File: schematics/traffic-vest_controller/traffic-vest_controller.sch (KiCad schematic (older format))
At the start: 21 parts

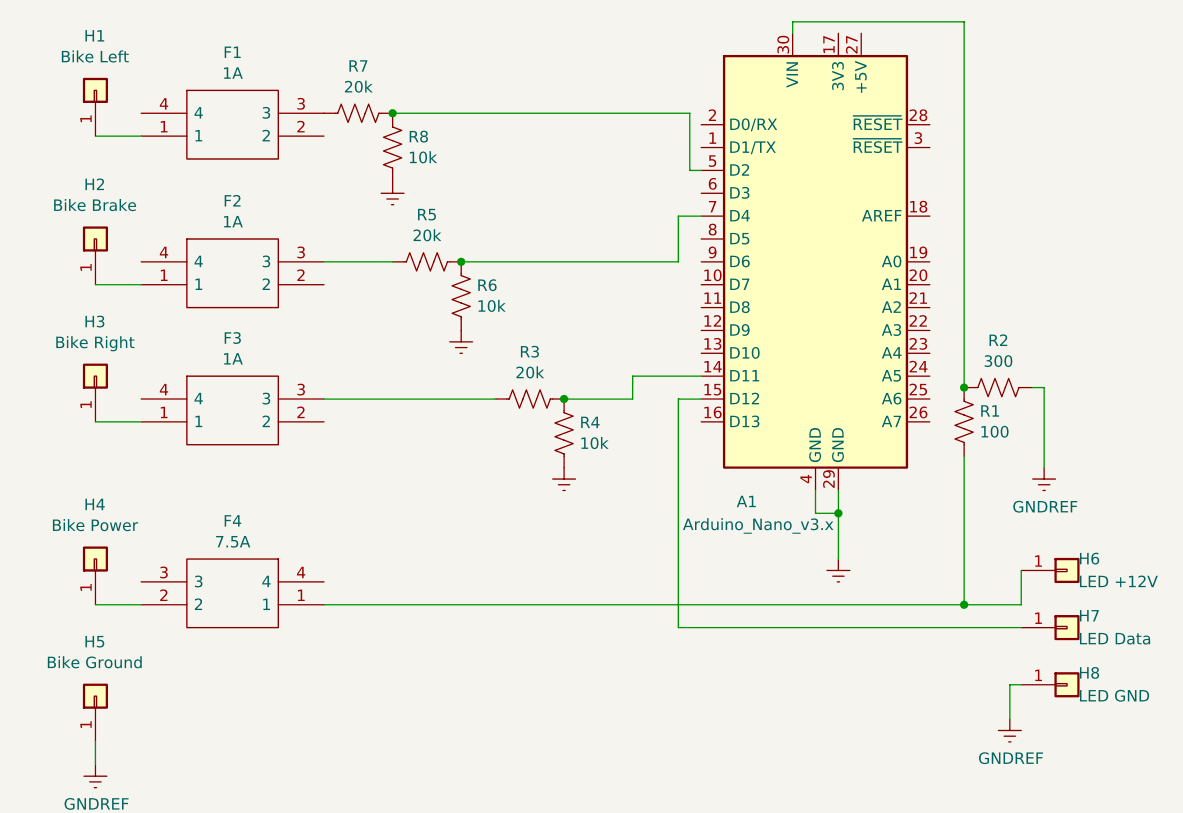
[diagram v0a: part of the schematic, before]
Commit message: expanded board footprint to accomodate corner mounting holes; rearranged fuses and pins for left/right to D2, D3 for external interrupts; fixed orientation of fuse clips
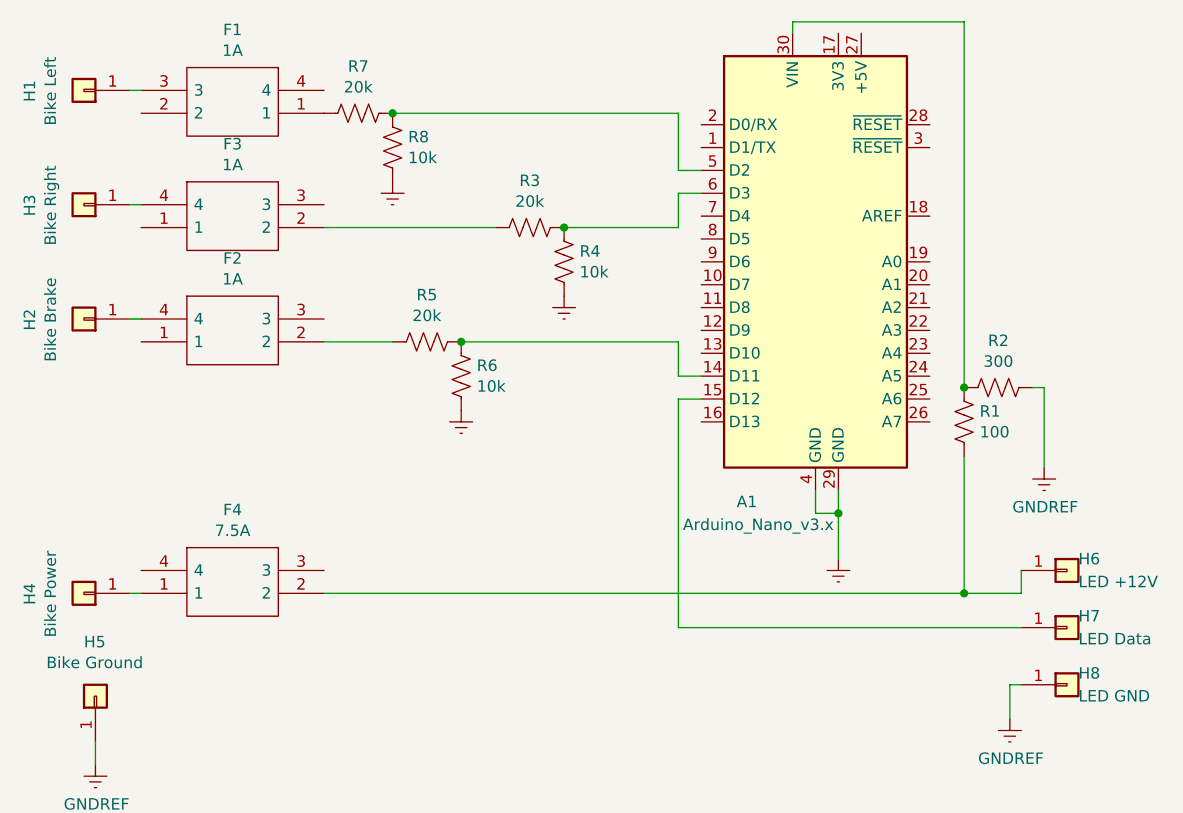
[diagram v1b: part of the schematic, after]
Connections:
- net at R3.1, R4.1: now also A1.6 (D3); no longer A1.14 (D11)
- net at R5.1, R6.1: now also A1.14 (D11); no longer A1.7 (D4)
- net at R7.2: now also F1.1; no longer F1.3
- net at R5.2: now also F2.2; no longer F2.3
- net at R3.2: now also F3.2; no longer F3.3
- net at H6.1 (Pin_1), R1.2: now also F4.2; no longer F4.1
- net at H1.1 (Pin_1): now also F1.3; no longer F1.1
- net at F2.1: no longer H2.1 (Pin_1)
- net at F2.4: now also H2.1 (Pin_1)
- net at F3.1: no longer H3.1 (Pin_1)
- net at F3.4: now also H3.1 (Pin_1)
- net at H4.1 (Pin_1): now also F4.1; no longer F4.2
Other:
- moved on the sheet: F1, F2, F3, F4, H1, H2, H3, H4, R3, R4, R5, R6

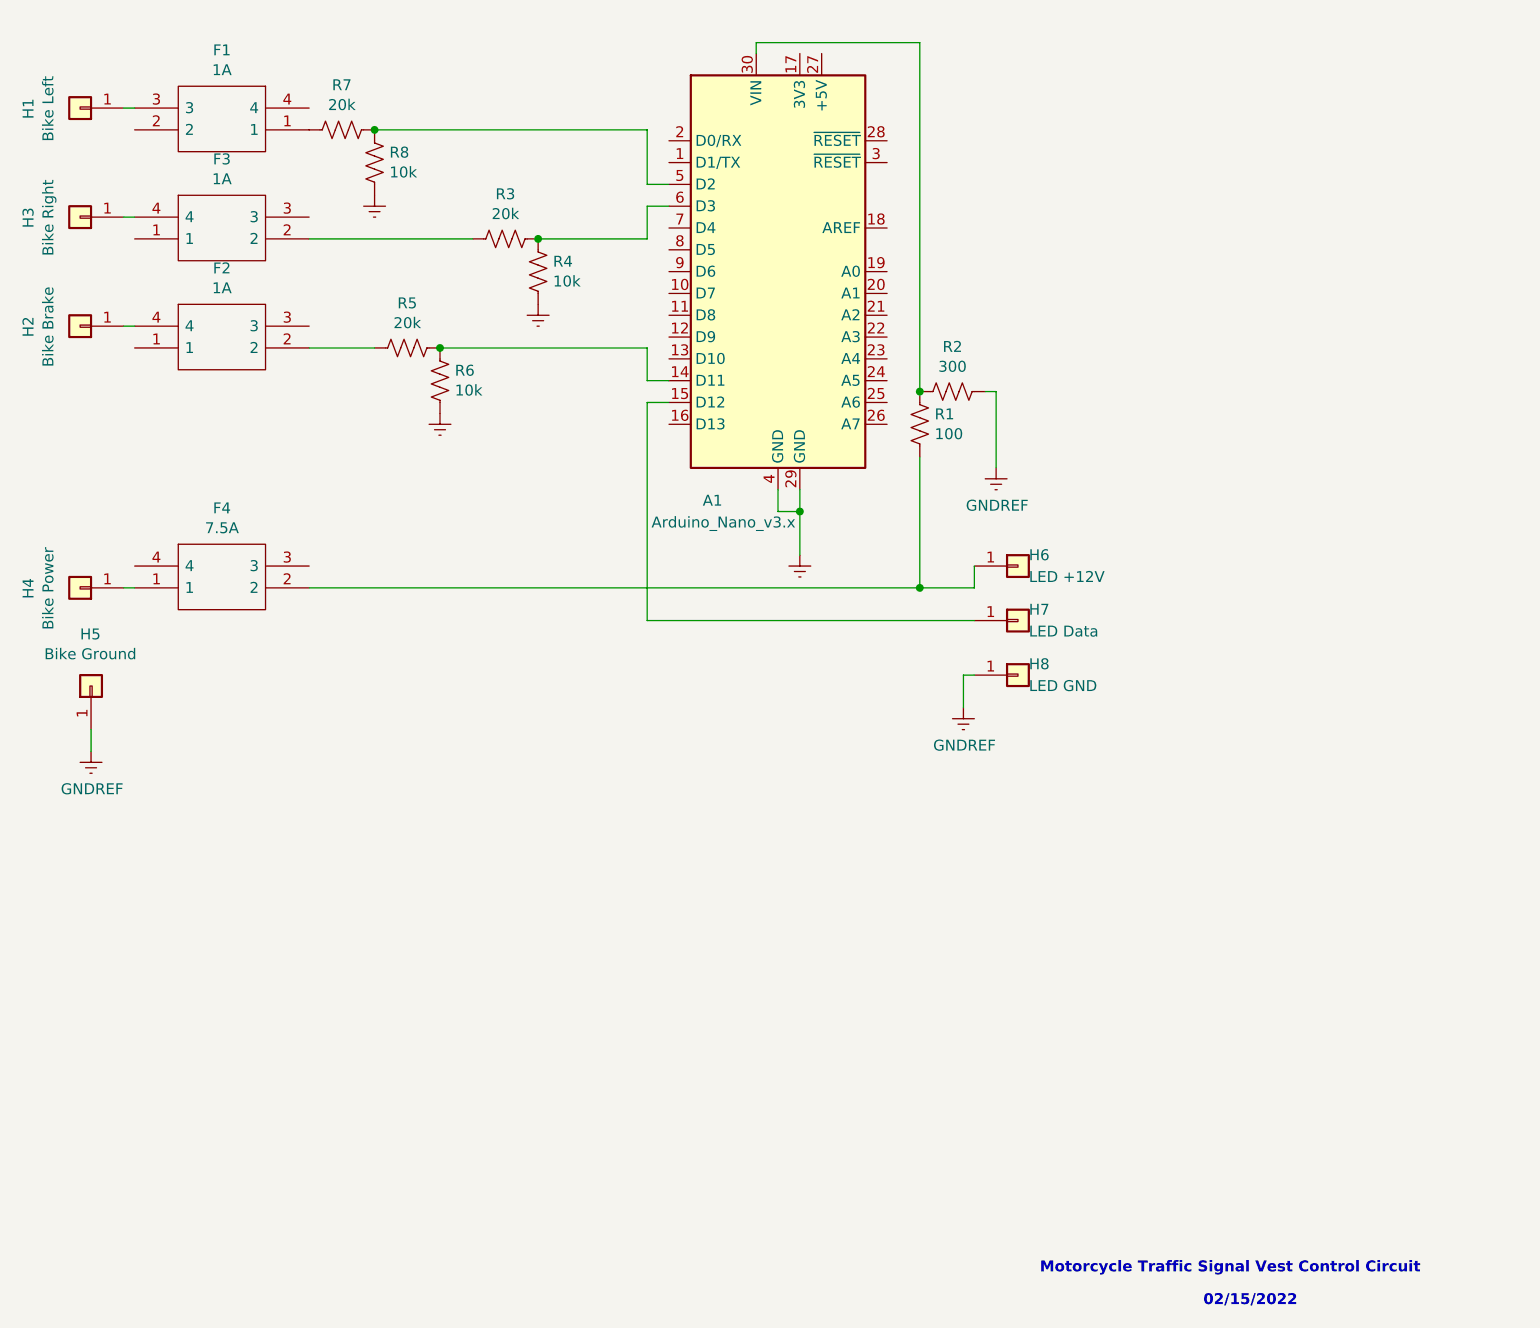
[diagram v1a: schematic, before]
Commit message: moved copper to back of PCB, flipped fuse clips, rerouted tracks, refilled copper pour
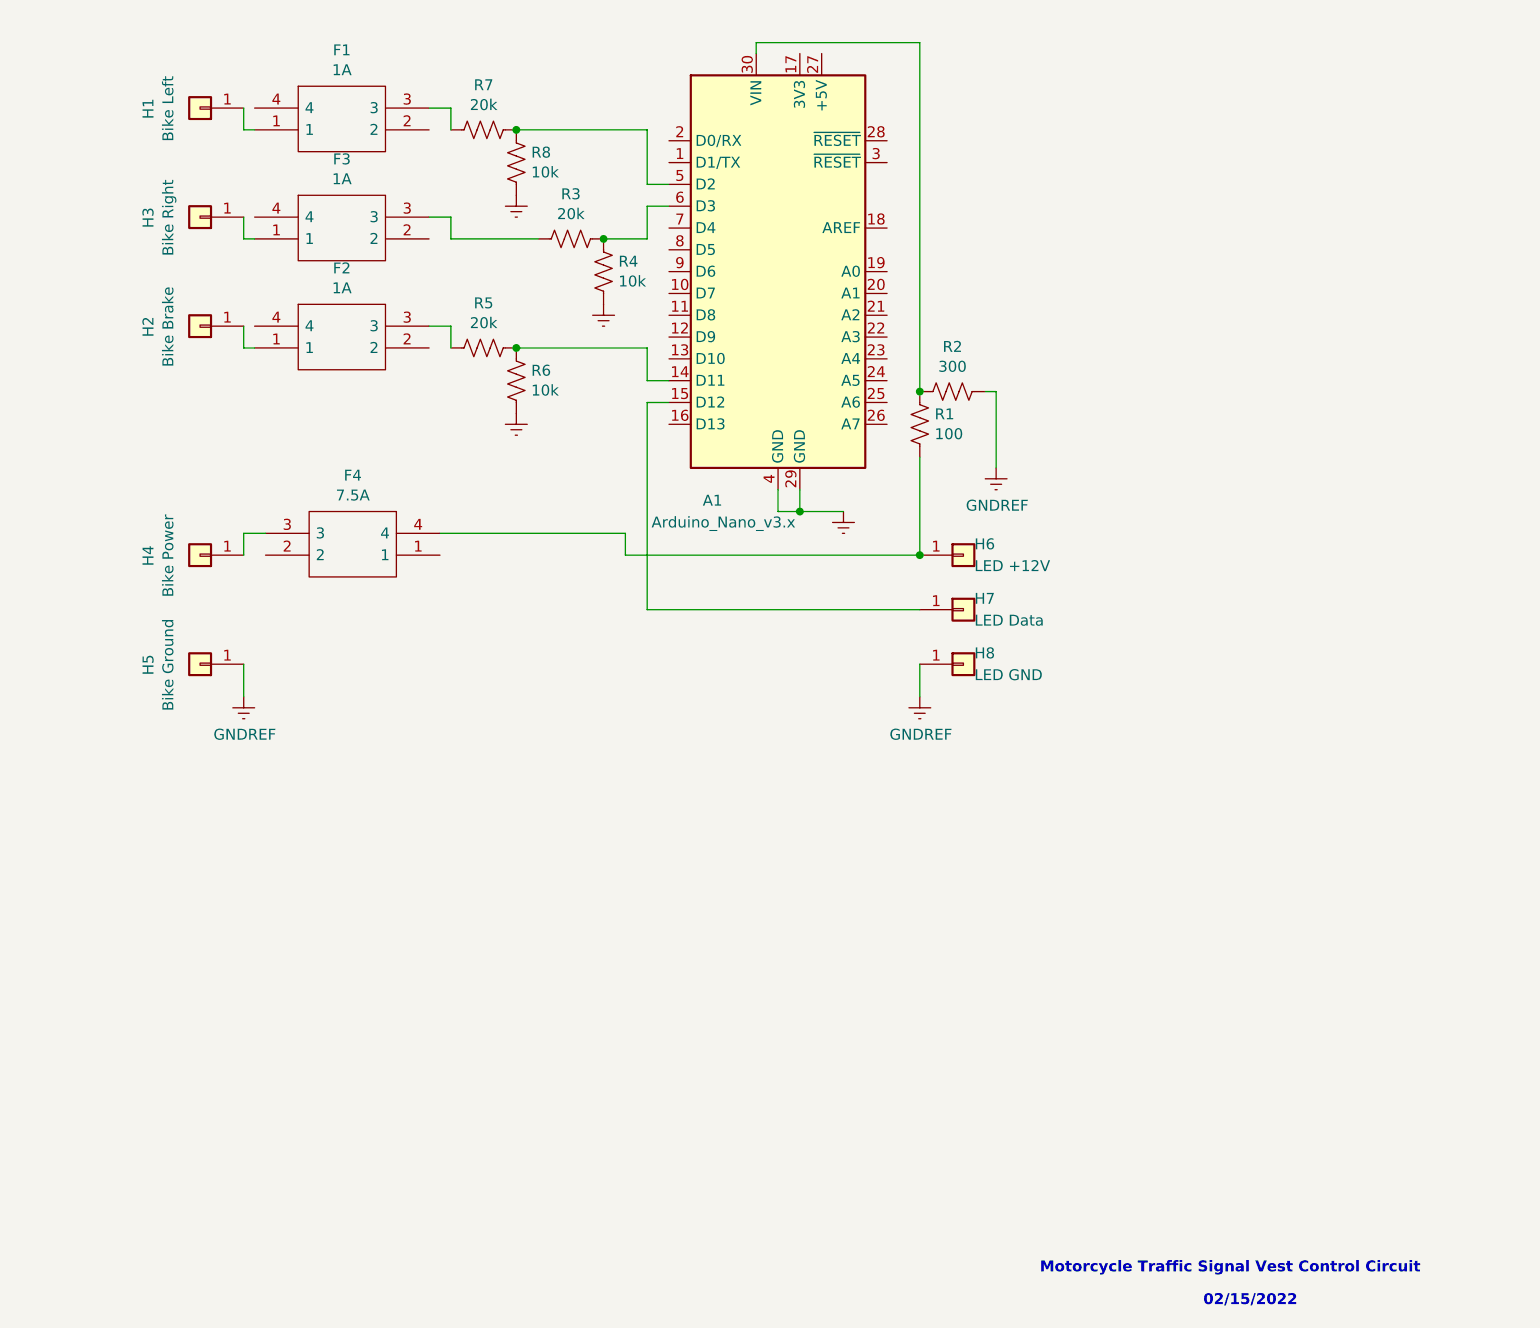
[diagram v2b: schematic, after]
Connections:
- net at R7.2: now also F1.3; no longer F1.1
- net at R5.2: now also F2.3; no longer F2.2
- net at R3.2: now also F3.3; no longer F3.2
- net at H6.1 (Pin_1), R1.2: now also F4.4; no longer F4.2
- net at H1.1 (Pin_1): now also F1.1; no longer F1.3
- net at F2.1: now also H2.1 (Pin_1)
- net at F2.4: no longer H2.1 (Pin_1)
- net at F3.1: now also H3.1 (Pin_1)
- net at F3.4: no longer H3.1 (Pin_1)
- net at F4.1: no longer H4.1 (Pin_1)
- net at F4.3: now also H4.1 (Pin_1)
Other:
- moved on the sheet: F1, F2, F3, F4, H1, H2, H3, H4, H5, H6, H7, H8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
